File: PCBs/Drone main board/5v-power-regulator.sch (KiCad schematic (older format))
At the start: 6 parts, among them U301 AP63205WU-7

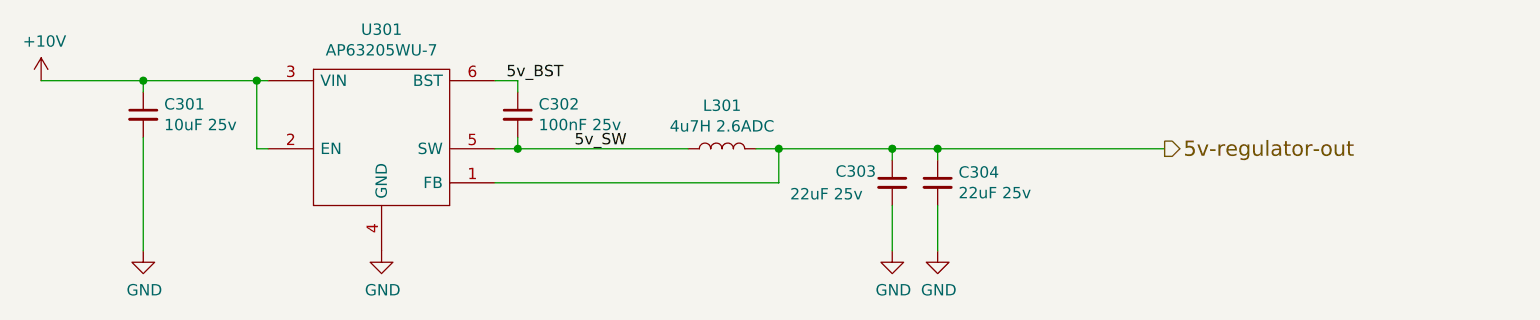
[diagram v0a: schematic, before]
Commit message: Some cleanup, and PCB antenna removal.
Last edits before asking for reddit feedback.

Signed-off-by: Eldalote.Electronics <Eldalote.Electronics@gmail.com>
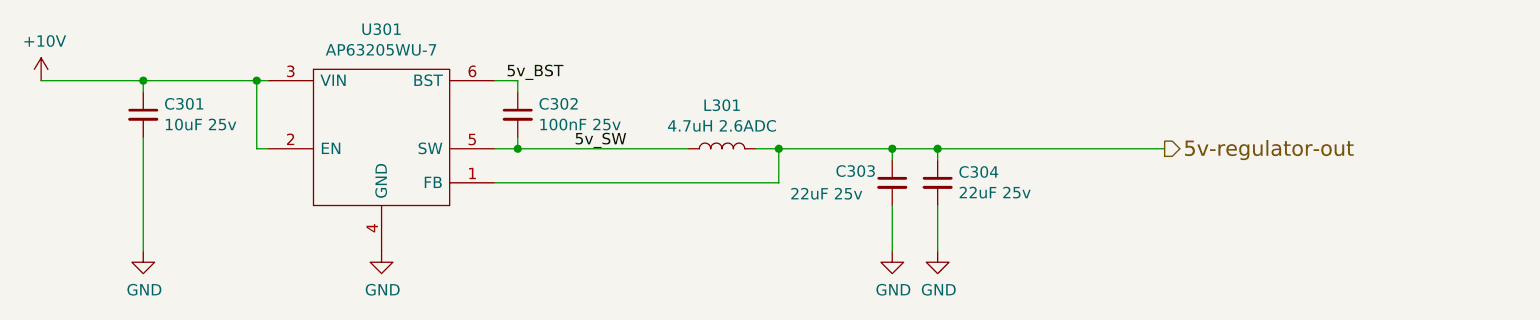
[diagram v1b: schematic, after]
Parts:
- L301: value 4u7H 2.6ADC -> 4.7uH 2.6ADC
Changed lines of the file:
@@
 P 5900 3450
 F 0 "L301" V 6090 3450 50  0000 C CNN
-F 1 "4u7H 2.6ADC" V 5999 3450 50  0000 C CNN
+F 1 "4.7uH 2.6ADC" V 5999 3450 50  0000 C CNN
 F 2 "Eldalote-footprints:L_5030_TAIYO_YUDEN" H 5900 3450 50  0001 C CNN
 F 3 "~" H 5900 3450 50  0001 C CNN

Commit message: Started to recheck components, and make a better BOM.
Signed-off-by: Eldalote.Electronics <Eldalote.Electronics@gmail.com>
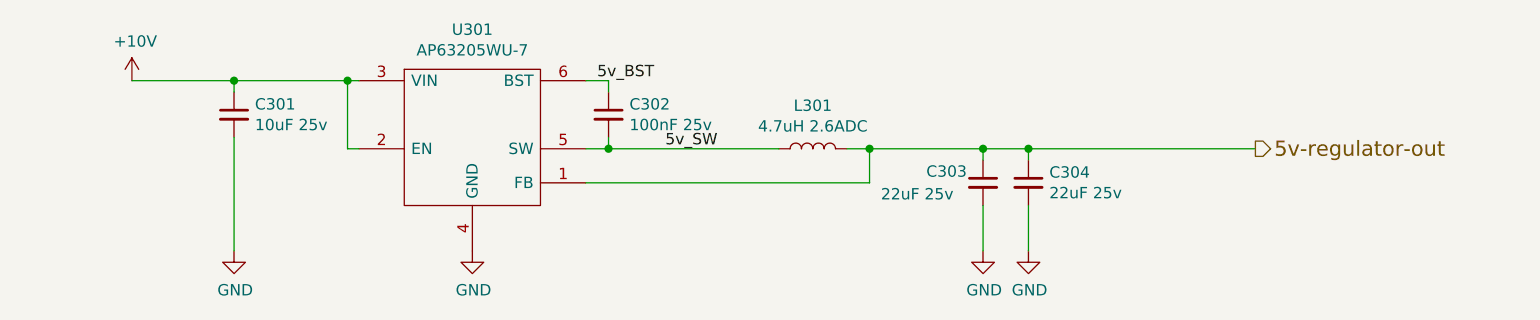
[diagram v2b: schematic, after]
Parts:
- C301: footprint Capacitor_SMD:C_0805_2012Metric_Pad1.15x1.40mm_HandSolder -> Capacitor_SMD:C_0805_2012Metric; DigiKey 1276-6454-1-ND -> (none); LCSC C15850 -> (none); MfNr (none) -> CL21A106KAYNNNG; Mouser 187-CL21A106KAYNNNG -> (none)
- C302: footprint Capacitor_SMD:C_0805_2012Metric_Pad1.15x1.40mm_HandSolder -> Capacitor_SMD:C_0805_2012Metric; DigiKey 1276-1099-1-ND -> (none); LCSC C49678 -> (none); MfNr (none) -> CL21B104KACNNNC; Mouser 187-CL21B104KACNNNC -> (none)
- C303, C304: footprint Capacitor_SMD:C_0805_2012Metric_Pad1.15x1.40mm_HandSolder -> Capacitor_SMD:C_0805_2012Metric; DigiKey 1276-2908-1-ND -> (none); LCSC C45783 -> (none); MfNr (none) -> CL21A226MAQNNNE; Mouser 187-CL21A226MAQNNNE -> (none)
- L301: DigiKey 587-3461-1-ND -> (none); MfNR (none) -> NRS5030T4R7MMGJ; Mouser 963-NRS5030T4R7MMGJ -> (none)
- U301: DigiKey AP63205WU-7DICT-ND -> (none); MfNr (none) -> AP63205WU-7; Mouser 621-AP63205WU-7 -> (none)
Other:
- moved on the sheet: C301, C302, C303, C304, L301, U301
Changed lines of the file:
@@
 Comment4 ""
 $EndDescr
-Text HLabel 7850 3450 2    67   Output ~ 0
+Text HLabel 8250 3450 2    67   Output ~ 0
 5v-regulator-out
 $Comp
 L SamacSys_Parts:AP63205WU-7 U301
 U 1 1 5F62701B
-P 3900 3200
-F 0 "U301" H 4400 3475 50  0000 C CNN
-F 1 "AP63205WU-7" H 4400 3384 50  0000 C CNN
-F 2 "SOT95P280X100-6N" H 4750 3300 50  0001 L CNN
-F 3 "https://www.diodes.com/assets/Datasheets/AP63200-AP63201-AP63203-AP63205.pdf" H 4750 3200 50  0001 L CNN
-F 4 "Switching Voltage Regulators DCDC Conv HV Buck TSOT26 T&R 3K" H 4750 3100 50  0001 L CNN "Description"
-F 5 "621-AP63205WU-7" H 4750 2900 50  0001 L CNN "Mouser"
-F 6 "AP63205WU-7DICT-ND " H 3900 3200 50  0001 C CNN "DigiKey"
-	1    3900 3200
+P 4300 3200
+F 0 "U301" H 4800 3475 50  0000 C CNN
+F 1 "AP63205WU-7" H 4800 3384 50  0000 C CNN
+F 2 "SOT95P280X100-6N" H 5150 3300 50  0001 L CNN
+F 3 "https://www.diodes.com/assets/Datasheets/AP63200-AP63201-AP63203-AP63205.pdf" H 5150 3200 50  0001 L CNN
+F 4 "Switching Voltage Regulators DCDC Conv HV Buck TSOT26 T&R 3K" H 5150 3100 50  0001 L CNN "Description"
+F 5 "AP63205WU-7" H 4300 3200 50  0001 C CNN "MfNr"
+	1    4300 3200
 	1    0    0    -1
 $EndComp
@@
 L Device:L L301
 U 1 1 5F6280C9
-P 5900 3450
-F 0 "L301" V 6090 3450 50  0000 C CNN
-F 1 "4.7uH 2.6ADC" V 5999 3450 50  0000 C CNN
-F 2 "Eldalote-footprints:L_5030_TAIYO_YUDEN" H 5900 3450 50  0001 C CNN
-F 3 "~" H 5900 3450 50  0001 C CNN
-F 4 "963-NRS5030T4R7MMGJ" V 5900 3450 50  0001 C CNN "Mouser"
-F 5 "587-3461-1-ND " V 5900 3450 50  0001 C CNN "DigiKey"
-	1    5900 3450
+P 6300 3450
+F 0 "L301" V 6490 3450 50  0000 C CNN
+F 1 "4.7uH 2.6ADC" V 6399 3450 50  0000 C CNN
+F 2 "Eldalote-footprints:L_5030_TAIYO_YUDEN" H 6300 3450 50  0001 C CNN
+F 3 "~" H 6300 3450 50  0001 C CNN
+F 4 "NRS5030T4R7MMGJ" V 6300 3450 50  0001 C CNN "MfNR"
+	1    6300 3450
 	0    -1   -1   0
 $EndComp
@@
 L Device:C_Small C302
 U 1 1 5F628DE0
-P 5000 3300
-F 0 "C302" H 5092 3346 50  0000 L CNN
-F 1 "100nF 25v" H 5092 3255 50  0000 L CNN
-F 2 "Capacitor_SMD:C_0805_2012Metric_Pad1.15x1.40mm_HandSolder" H 5000 3300 50  0001 C CNN
-F 3 "~" H 5000 3300 50  0001 C CNN
-F 4 "C49678" H 5000 3300 50  0001 C CNN "LCSC"
-F 5 "1276-1099-1-ND " H 5000 3300 50  0001 C CNN "DigiKey"
-F 6 "187-CL21B104KACNNNC " H 5000 3300 50  0001 C CNN "Mouser"
-	1    5000 3300
+P 5400 3300
+F 0 "C302" H 5492 3346 50  0000 L CNN
+F 1 "100nF 25v" H 5492 3255 50  0000 L CNN
+F 2 "Capacitor_SMD:C_0805_2012Metric" H 5400 3300 50  0001 C CNN
+F 3 "~" H 5400 3300 50  0001 C CNN
+F 4 "CL21B104KACNNNC" H 5400 3300 50  0001 C CNN "MfNr"
+	1    5400 3300
 	1    0    0    -1
 $EndComp
@@
 L Device:C_Small C301
 U 1 1 5F629D01
-P 3350 3300
-F 0 "C301" H 3442 3346 50  0000 L CNN
-F 1 "10uF 25v" H 3442 3255 50  0000 L CNN
-F 2 "Capacitor_SMD:C_0805_2012Metric_Pad1.15x1.40mm_HandSolder" H 3350 3300 50  0001 C CNN
-F 3 "~" H 3350 3300 50  0001 C CNN
-F 4 "C15850" H 3350 3300 50  0001 C CNN "LCSC"
-F 5 "1276-6454-1-ND" H 3350 3300 50  0001 C CNN "DigiKey"
-F 6 " 187-CL21A106KAYNNNG " H 3350 3300 50  0001 C CNN "Mouser"
-	1    3350 3300
+P 3750 3300
+F 0 "C301" H 3842 3346 50  0000 L CNN
+F 1 "10uF 25v" H 3842 3255 50  0000 L CNN
+F 2 "Capacitor_SMD:C_0805_2012Metric" H 3750 3300 50  0001 C CNN
+F 3 "~" H 3750 3300 50  0001 C CNN
+F 4 "CL21A106KAYNNNG" H 3750 3300 50  0001 C CNN "MfNr"
+	1    3750 3300
 	1    0    0    -1
 $EndComp
@@
 L Device:C_Small C303
 U 1 1 5F62A1BB
-P 6650 3600
-F 0 "C303" H 6400 3650 50  0000 L CNN
-F 1 "22uF 25v" H 6200 3550 50  0000 L CNN
-F 2 "Capacitor_SMD:C_0805_2012Metric_Pad1.15x1.40mm_HandSolder" H 6650 3600 50  0001 C CNN
-F 3 "~" H 6650 3600 50  0001 C CNN
-F 4 "C45783" H 6650 3600 50  0001 C CNN "LCSC"
-F 5 "1276-2908-1-ND " H 6650 3600 50  0001 C CNN "DigiKey"
-F 6 " 187-CL21A226MAQNNNE " H 6650 3600 50  0001 C CNN "Mouser"
-	1    6650 3600
+P 7050 3600
+F 0 "C303" H 6800 3650 50  0000 L CNN
+F 1 "22uF 25v" H 6600 3550 50  0000 L CNN
+F 2 "Capacitor_SMD:C_0805_2012Metric" H 7050 3600 50  0001 C CNN
+F 3 "~" H 7050 3600 50  0001 C CNN
+F 4 "CL21A226MAQNNNE" H 7050 3600 50  0001 C CNN "MfNr"
+	1    7050 3600
 	1    0    0    -1
 $EndComp
@@
 L Device:C_Small C304
 U 1 1 5F62AF34
-P 6850 3600
-F 0 "C304" H 6942 3646 50  0000 L CNN
-F 1 "22uF 25v" H 6942 3555 50  0000 L CNN
-F 2 "Capacitor_SMD:C_0805_2012Metric_Pad1.15x1.40mm_HandSolder" H 6850 3600 50  0001 C CNN
-F 3 "~" H 6850 3600 50  0001 C CNN
-F 4 "C45783" H 6850 3600 50  0001 C CNN "LCSC"
-F 5 "1276-2908-1-ND " H 6850 3600 50  0001 C CNN "DigiKey"
-F 6 " 187-CL21A226MAQNNNE " H 6850 3600 50  0001 C CNN "Mouser"
-	1    6850 3600
+P 7250 3600
+F 0 "C304" H 7342 3646 50  0000 L CNN
+F 1 "22uF 25v" H 7342 3555 50  0000 L CNN
+F 2 "Capacitor_SMD:C_0805_2012Metric" H 7250 3600 50  0001 C CNN
+F 3 "~" H 7250 3600 50  0001 C CNN
+F 4 "CL21A226MAQNNNE" H 7250 3600 50  0001 C CNN "MfNr"
+	1    7250 3600
 	1    0    0    -1
 $EndComp
 Wire Wire Line
-	4900 3450 5000 3450
+	5300 3450 5400 3450
 Wire Wire Line
-	5000 3400 5000 3450
-Connection ~ 5000 3450
+	5400 3400 5400 3450
+Connection ~ 5400 3450
 Wire Wire Line
-	5000 3450 5750 3450
+	5400 3450 6150 3450
 Wire Wire Line
-	5000 3200 5000 3150
+	5400 3200 5400 3150
 Wire Wire Line
-	5000 3150 4900 3150
+	5400 3150 5300 3150
 Wire Wire Line
-	3900 3150 3850 3150
+	4300 3150 4250 3150
 Wire Wire Line
-	3350 3150 3350 3200
+	3750 3150 3750 3200
 Wire Wire Line
-	3350 3150 2900 3150
-Connection ~ 3350 3150
+	3750 3150 3300 3150
+Connection ~ 3750 3150
 Wire Wire Line
-	3900 3450 3850 3450
+	4300 3450 4250 3450
 Wire Wire Line
-	3850 3450 3850 3150
-Connection ~ 3850 3150
+	4250 3450 4250 3150
+Connection ~ 4250 3150
 Wire Wire Line
-	3850 3150 3350 3150
+	4250 3150 3750 3150
 Wire Wire Line
-	3350 3400 3350 3900
+	3750 3400 3750 3900
 Wire Wire Line
-	6050 3450 6150 3450
+	6450 3450 6550 3450
 Wire Wire Line
-	6650 3450 6650 3500
-Connection ~ 6650 3450
+	7050 3450 7050 3500
+Connection ~ 7050 3450
 Wire Wire Line
-	6650 3450 6850 3450
+	7050 3450 7250 3450
 Wire Wire Line
-	6850 3450 6850 3500
-Connection ~ 6850 3450
+	7250 3450 7250 3500
+Connection ~ 7250 3450
 Wire Wire Line
-	6850 3450 7850 3450
+	7250 3450 8250 3450
 Wire Wire Line
-	6650 3700 6650 3900
+	7050 3700 7050 3900
 Wire Wire Line
-	6850 3700 6850 3900
+	7250 3700 7250 3900
 Wire Wire Line
-	4900 3600 6150 3600
+	5300 3600 6550 3600
 Wire Wire Line
-	6150 3600 6150 3450
-Connection ~ 6150 3450
+	6550 3600 6550 3450
+Connection ~ 6550 3450
 Wire Wire Line
-	6150 3450 6650 3450
+	6550 3450 7050 3450
 $Comp
 L power:+10V #PWR0301
 U 1 1 5F62DA8E
-P 2900 3150
-F 0 "#PWR0301" H 2900 3000 50  0001 C CNN
-F 1 "+10V" H 2915 3323 50  0000 C CNN
-F 2 "" H 2900 3150 50  0001 C CNN
-F 3 "" H 2900 3150 50  0001 C CNN
-	1    2900 3150
+P 3300 3150
+F 0 "#PWR0301" H 3300 3000 50  0001 C CNN
+F 1 "+10V" H 3315 3323 50  0000 C CNN
+F 2 "" H 3300 3150 50  0001 C CNN
+F 3 "" H 3300 3150 50  0001 C CNN
+	1    3300 3150
 	1    0    0    -1
 $EndComp
@@
 L power:GND #PWR0302
 U 1 1 5F62DFB0
-P 3350 3900
-F 0 "#PWR0302" H 3350 3650 50  0001 C CNN
-F 1 "GND" H 3355 3727 50  0000 C CNN
-F 2 "" H 3350 3900 50  0001 C CNN
-F 3 "" H 3350 3900 50  0001 C CNN
-	1    3350 3900
+P 3750 3900
+F 0 "#PWR0302" H 3750 3650 50  0001 C CNN
+F 1 "GND" H 3755 3727 50  0000 C CNN
+F 2 "" H 3750 3900 50  0001 C CNN
+F 3 "" H 3750 3900 50  0001 C CNN
+	1    3750 3900
 	1    0    0    -1
 $EndComp
@@
 L power:GND #PWR0303
 U 1 1 5F62E4B9
-P 4400 3900
-F 0 "#PWR0303" H 4400 3650 50  0001 C CNN
-F 1 "GND" H 4405 3727 50  0000 C CNN
-F 2 "" H 4400 3900 50  0001 C CNN
-F 3 "" H 4400 3900 50  0001 C CNN
-	1    4400 3900
+P 4800 3900
+F 0 "#PWR0303" H 4800 3650 50  0001 C CNN
+F 1 "GND" H 4805 3727 50  0000 C CNN
+F 2 "" H 4800 3900 50  0001 C CNN
+F 3 "" H 4800 3900 50  0001 C CNN
+	1    4800 3900
 	1    0    0    -1
 $EndComp
@@
 L power:GND #PWR0304
 U 1 1 5F62E6DC
-P 6650 3900
-F 0 "#PWR0304" H 6650 3650 50  0001 C CNN
-F 1 "GND" H 6655 3727 50  0000 C CNN
-F 2 "" H 6650 3900 50  0001 C CNN
-F 3 "" H 6650 3900 50  0001 C CNN
-	1    6650 3900
+P 7050 3900
+F 0 "#PWR0304" H 7050 3650 50  0001 C CNN
+F 1 "GND" H 7055 3727 50  0000 C CNN
+F 2 "" H 7050 3900 50  0001 C CNN
+F 3 "" H 7050 3900 50  0001 C CNN
+	1    7050 3900
 	1    0    0    -1
 $EndComp
@@
 L power:GND #PWR0305
 U 1 1 5F62EA06
-P 6850 3900
-F 0 "#PWR0305" H 6850 3650 50  0001 C CNN
-F 1 "GND" H 6855 3727 50  0000 C CNN
-F 2 "" H 6850 3900 50  0001 C CNN
-F 3 "" H 6850 3900 50  0001 C CNN
-	1    6850 3900
+P 7250 3900
+F 0 "#PWR0305" H 7250 3650 50  0001 C CNN
+F 1 "GND" H 7255 3727 50  0000 C CNN
+F 2 "" H 7250 3900 50  0001 C CNN
+F 3 "" H 7250 3900 50  0001 C CNN
+	1    7250 3900
 	1    0    0    -1
 $EndComp
-Text Label 4950 3150 0    50   ~ 0
+Text Label 5350 3150 0    50   ~ 0
 5v_BST
-Text Label 5250 3450 0    50   ~ 0
+Text Label 5650 3450 0    50   ~ 0
 5v_SW
 $EndSCHEMATC

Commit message: Lots of work to check every component, add Manufacturers number (instead of LCSC or digikey and mouser numbers)
Changed to USB-C connector, almost done with that sheet. Components checked, need to redo Sheet IO

Signed-off-by: Eldalote.Electronics <Eldalote.Electronics@gmail.com>
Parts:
- L301: MfNR NRS5030T4R7MMGJ -> (none); MfNr (none) -> NRS5030T4R7MMGJ
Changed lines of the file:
@@
 F 2 "Eldalote-footprints:L_5030_TAIYO_YUDEN" H 6300 3450 50  0001 C CNN
 F 3 "~" H 6300 3450 50  0001 C CNN
-F 4 "NRS5030T4R7MMGJ" V 6300 3450 50  0001 C CNN "MfNR"
+F 4 "" V 6300 3450 50  0001 C CNN "MfNR"
+F 5 "NRS5030T4R7MMGJ" H 6300 3450 50  0001 C CNN "MfNr"
 	1    6300 3450
 	0    -1   -1   0
